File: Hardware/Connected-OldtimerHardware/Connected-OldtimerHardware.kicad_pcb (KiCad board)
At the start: 2 copper layers, 113 x 58 mm, 27 parts, among them J1 NextionConnector, J2 MainConnector, J3 CAN_Bus_Connector, J4 AUXConnector, Q1 2N3906, U1 ParticleElectron, U2 TSR_2-2450, U3 CANTranceiverModule, U4 AdafruitFRAM, U5 AdafruitUltimateGPS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

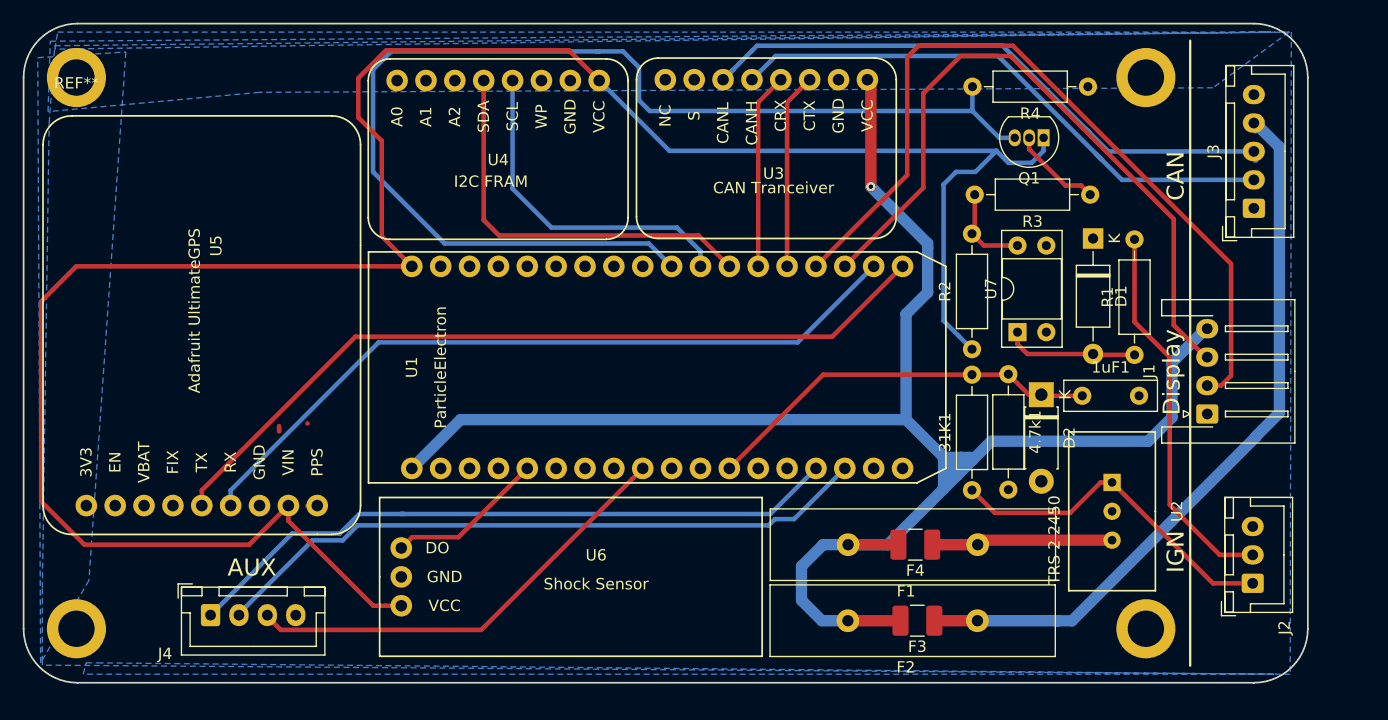
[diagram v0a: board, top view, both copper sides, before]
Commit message: switched to horizontal plugs
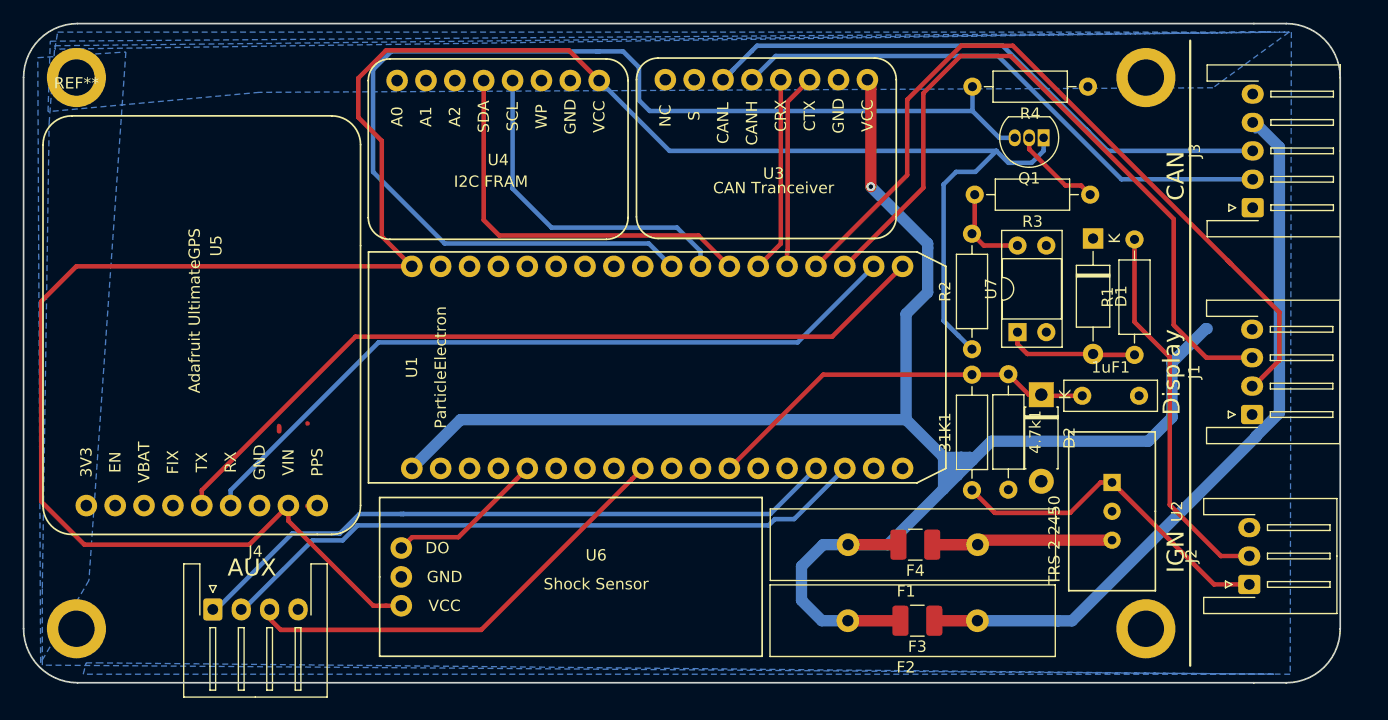
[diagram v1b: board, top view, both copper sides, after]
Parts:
- J2: footprint Connector_JST:JST_XH_B03B-XH-A_1x03_P2.50mm_Vertical -> Connector_JST:JST_XH_S03B-XH-A-1_1x03_P2.50mm_Horizontal
- J3: footprint Connector_JST:JST_XH_B05B-XH-A_1x05_P2.50mm_Vertical -> Connector_JST:JST_XH_S05B-XH-A-1_1x05_P2.50mm_Horizontal
- J4: footprint Connector_JST:JST_XH_B04B-XH-A_1x04_P2.50mm_Vertical -> Connector_JST:JST_XH_S04B-XH-A-1_1x04_P2.50mm_Horizontal
- moved J1 3.95 mm to (199.8, 96.7)
- moved J4 0.54 mm to (108.4, 113.8)
- moved J2 0.32 mm to (199.6, 111.6)
- moved J3 0.11 mm to (199.9, 78.5)
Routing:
- net Nextion_TX: track 60.9 -> 64.8 mm
- net CAN_H: track 50.2 -> 49.4 mm
- net Nextion_RX: track 71.0 -> 70.4 mm
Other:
- board size 113 x 58 mm -> 115.8 x 58 mm

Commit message: minor changes
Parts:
- moved J4 1.70 mm to (108.5, 112.1)
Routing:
- net AUX_2: track 58.7 -> 57.6 mm
- net AUX_1: track 58.9 -> 57.8 mm
- net AUX_3: track 39.5 -> 40.2 mm
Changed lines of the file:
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@@
     (thickness 1.6)
     (drawings 19)
-    (tracks 214)
+    (tracks 212)
     (zones 0)
     (modules 27)
@@
   )
   (module Connector_JST:JST_XH_S04B-XH-A-1_1x04_P2.50mm_Horizontal (layer F.Cu)
-    (at 108.4 113.8)
+    (at 108.45 112.1)
     (descr "JST XH series connector, S04B-XH-A-1 (http://www.jst-mfg.com/product/pdf/eng/eXH.pdf), generated with kicad-footprint-generator")
     (tags "connector JST XH top entry")
@@
   (segment (start 125.934999 107.445001) (end 130.014999 107.445001) (width 0.4) (layer F.Cu) (net 25))
   (segment (start 124.985 108.395) (end 125.934999 107.445001) (width 0.4) (layer F.Cu) (net 25))
-  (segment (start 108.2 114.3) (end 115.380001 107.119999) (width 0.4) (layer B.Cu) (net 40))
   (segment (start 157.46 105.4) (end 161.47 101.39) (width 0.4) (layer B.Cu) (net 40))
-  (segment (start 115.380001 107.119999) (end 119.580001 107.119999) (width 0.4) (layer B.Cu) (net 40))
+  (segment (start 124.9 105.4) (end 125.2 105.4) (width 0.4) (layer B.Cu) (net 40))
+  (segment (start 125.2 105.4) (end 157.46 105.4) (width 0.4) (layer B.Cu) (net 40))
   (segment (start 121.3 105.4) (end 125.2 105.4) (width 0.4) (layer B.Cu) (net 40))
   (segment (start 119.580001 107.119999) (end 121.3 105.4) (width 0.4) (layer B.Cu) (net 40))
-  (segment (start 124.9 105.4) (end 125.2 105.4) (width 0.4) (layer B.Cu) (net 40))
-  (segment (start 125.2 105.4) (end 157.46 105.4) (width 0.4) (layer B.Cu) (net 40))
-  (segment (start 110.7 114.175) (end 110.7 114.3) (width 0.4) (layer B.Cu) (net 41))
-  (segment (start 164.01 101.39) (end 159.54999 105.85001) (width 0.4) (layer B.Cu) (net 41))
-  (segment (start 157.858532 105.85001) (end 157.308542 106.4) (width 0.4) (layer B.Cu) (net 41))
-  (segment (start 159.54999 105.85001) (end 157.858532 105.85001) (width 0.4) (layer B.Cu) (net 41))
-  (segment (start 119.828533 107.720009) (end 117.175 107.720009) (width 0.4) (layer B.Cu) (net 41))
-  (segment (start 121.148542 106.4) (end 119.828533 107.720009) (width 0.4) (layer B.Cu) (net 41))
-  (segment (start 157.308542 106.4) (end 121.148542 106.4) (width 0.4) (layer B.Cu) (net 41))
-  (segment (start 117.175 107.7) (end 117.175 107.720009) (width 0.4) (layer B.Cu) (net 41))
-  (segment (start 117.175 107.720009) (end 110.7 114.175) (width 0.4) (layer B.Cu) (net 41))
+  (segment (start 108.45 112.1) (end 113.430001 107.119999) (width 0.4) (layer B.Cu) (net 40))
+  (segment (start 113.430001 107.119999) (end 119.580001 107.119999) (width 0.4) (layer B.Cu) (net 40))
+  (segment (start 159.54999 105.85001) (end 164.01 101.39) (width 0.4) (layer B.Cu) (net 41))
+  (segment (start 110.95 111.975) (end 114.775 108.15) (width 0.4) (layer B.Cu) (net 41))
+  (segment (start 110.95 112.1) (end 110.95 111.975) (width 0.4) (layer B.Cu) (net 41))
+  (segment (start 119.9 108.15) (end 121.65 106.4) (width 0.4) (layer B.Cu) (net 41))
+  (segment (start 114.775 108.15) (end 119.9 108.15) (width 0.4) (layer B.Cu) (net 41))
+  (segment (start 121.65 106.4) (end 159 106.4) (width 0.4) (layer B.Cu) (net 41))
+  (segment (start 159 106.4) (end 159.54999 105.85001) (width 0.4) (layer B.Cu) (net 41))
   (segment (start 145.280001 102.339999) (end 146.23 101.39) (width 0.4) (layer F.Cu) (net 42))
   (segment (start 132.01999 115.60001) (end 145.280001 102.339999) (width 0.4) (layer F.Cu) (net 42))
-  (segment (start 114.37501 115.60001) (end 132.01999 115.60001) (width 0.4) (layer F.Cu) (net 42))
-  (segment (start 113.2 114.425) (end 114.37501 115.60001) (width 0.4) (layer F.Cu) (net 42))
-  (segment (start 113.2 114.3) (end 113.2 114.425) (width 0.4) (layer F.Cu) (net 42))
+  (segment (start 116.82501 115.60001) (end 132.01999 115.60001) (width 0.4) (layer F.Cu) (net 42))
+  (segment (start 113.45 112.225) (end 116.82501 115.60001) (width 0.4) (layer F.Cu) (net 42))
+  (segment (start 113.45 112.1) (end 113.45 112.225) (width 0.4) (layer F.Cu) (net 42))
   (segment (start 162.1 93.14) (end 153.85 101.39) (width 0.4) (layer F.Cu) (net 55))
   (segment (start 175.2 93.14) (end 162.1 93.14) (width 0.4) (layer F.Cu) (net 55))

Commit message: Generated Gerbers
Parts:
- moved U4 0.11 mm to (131.0, 76.0)
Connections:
- net DAC renamed Net-(U1-Pad6)
- net RESET renamed Net-(U1-Pad35)
- net VBAT renamed Net-(U1-Pad34)
- J3 pad 5: Net-(J3-Pad5) -> 12VIN
- U1 pad 27: Net-(U1-Pad27) -> IGNSignal
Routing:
- net 12VIN: track 30.1 -> 81.4 mm
- net IGNSignal: track 103.0 -> 75.2 mm, vias 0 -> 2
- net 3V3: track 197.5 -> 203.9 mm
- net 5VDC: track 157.8 -> 161.9 mm
- net Net-(F2-Pad1): track 64.6 -> 67.5 mm
- net FRAM_SDA: track 35.6 -> 36.7 mm
- net FRAM_SCL: track 29.7 -> 30.7 mm
